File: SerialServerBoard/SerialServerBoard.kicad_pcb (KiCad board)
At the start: 2 copper layers, 60 parts, among them J1 3v3, J2 3v3_SW, J3 1v8, J4 1v35, J5 VCORE, J6 ASSMANN A-DF 09 A/KG-T2S, U1 SG2002, U2 MAX3237EIPWR

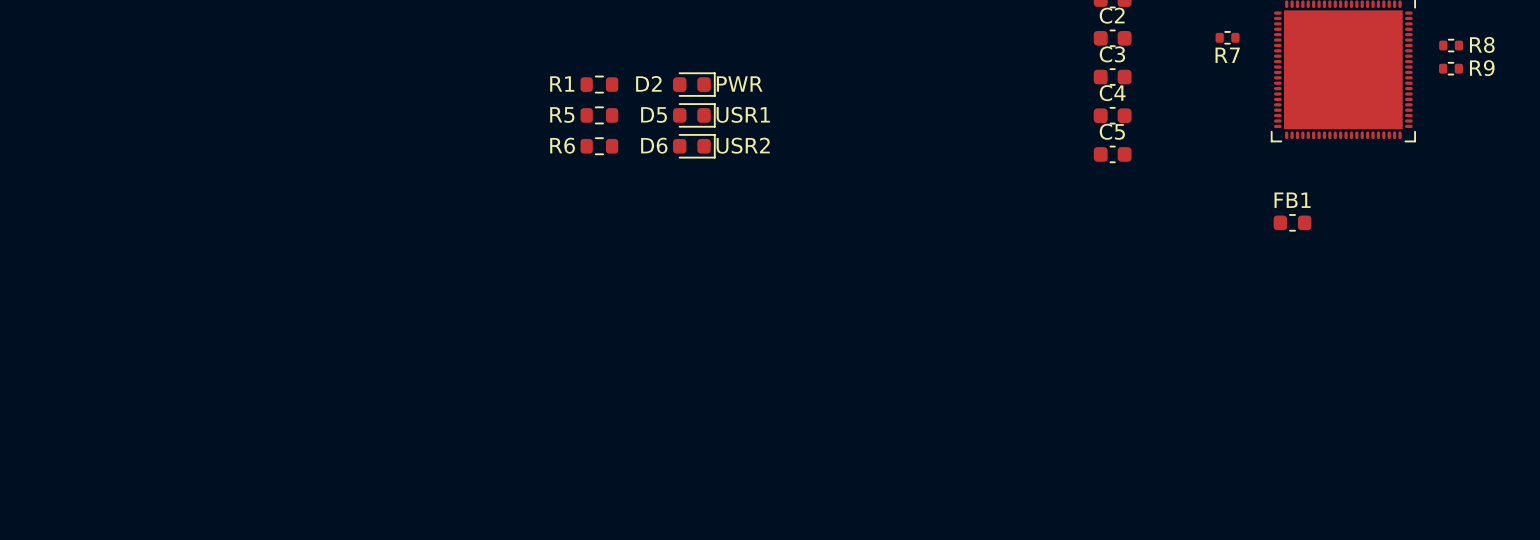
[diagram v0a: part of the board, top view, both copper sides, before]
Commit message: Add ATECC
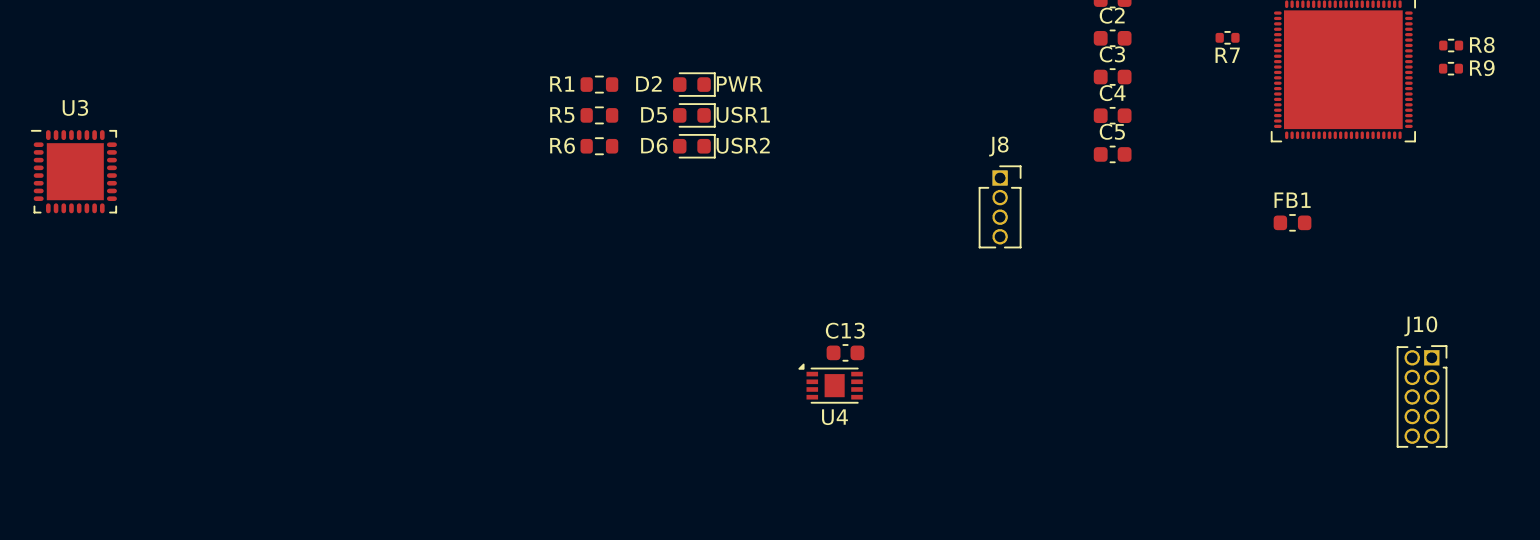
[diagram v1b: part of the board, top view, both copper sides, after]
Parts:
- added C13: TBD, Capacitor_SMD:C_0603_1608Metric, F.Cu at (101.2, 105.4)
- added J10: Conn_ARM_JTAG_SWD_10, Connector_PinSocket_1.27mm:PinSocket_2x05_P1.27mm_Vertical, F.Cu at (139.2, 105.7)
- added J8: ESP UART, Connector_PinSocket_1.27mm:PinSocket_1x04_P1.27mm_Vertical, F.Cu at (111.2, 94.1)
- added U3: ESP32-C3, Footprints:ESP32-C3, F.Cu at (51.2, 93.7)
- added U4: ATECC608B-MAHDA, Package_DFN_QFN:DFN-8-1EP_3x2mm_P0.5mm_EP1.3x1.5mm, F.Cu at (100.5, 107.5)

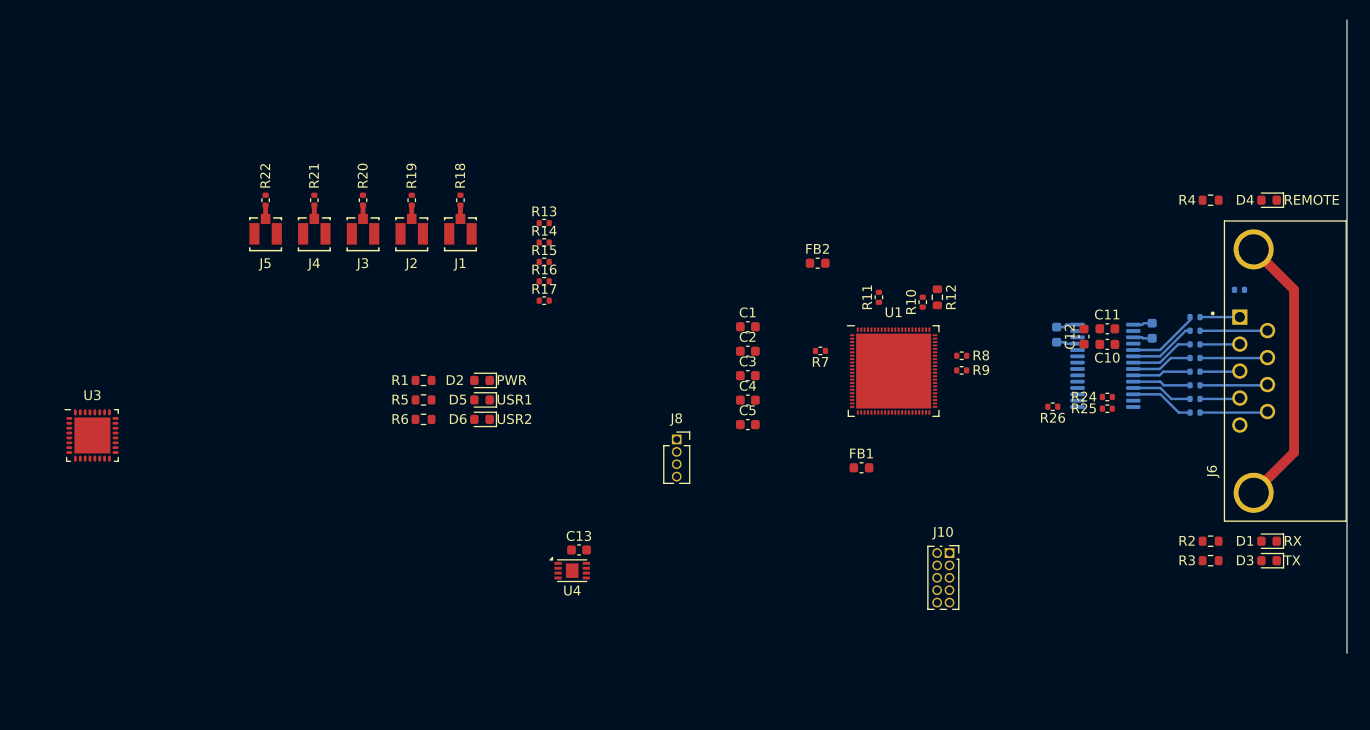
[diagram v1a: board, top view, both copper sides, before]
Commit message: Add micro-SD card slot
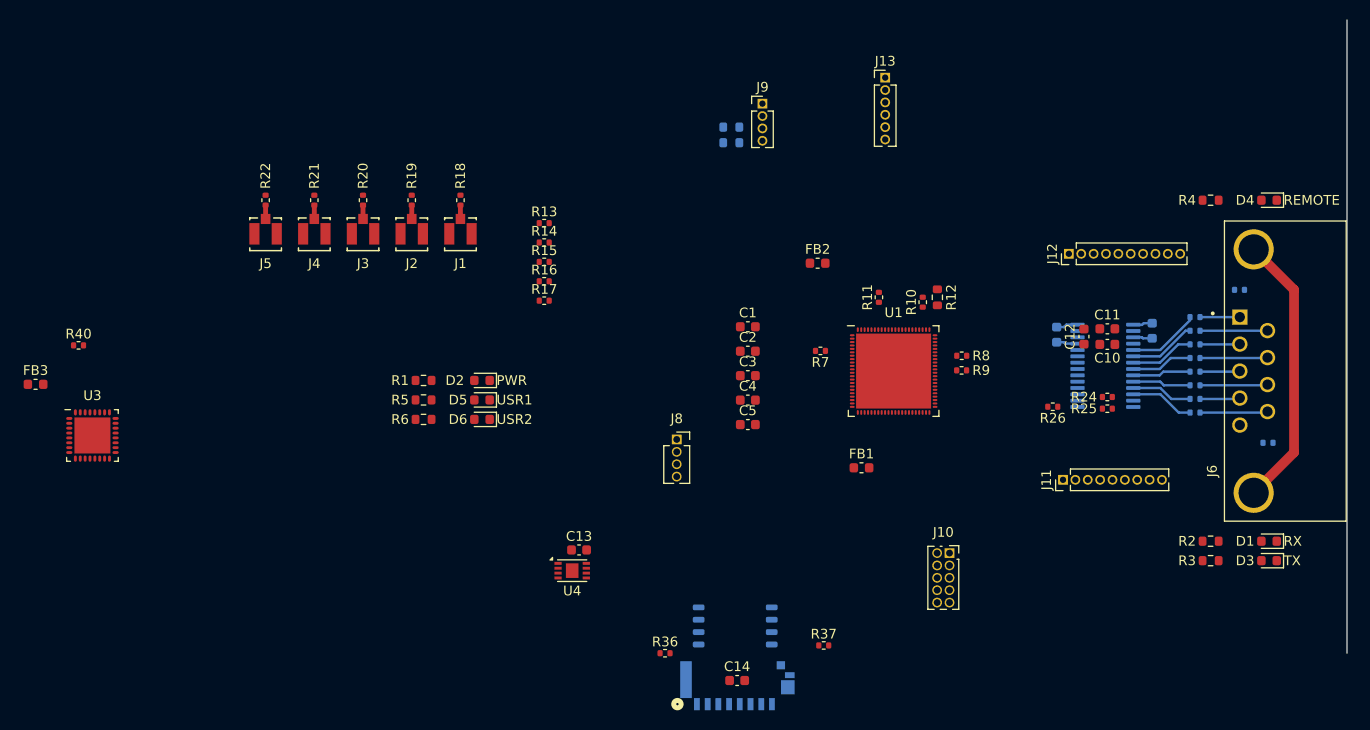
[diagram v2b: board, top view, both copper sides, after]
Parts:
- added C14: TBD, Capacitor_SMD:C_0603_1608Metric, F.Cu at (117.4, 118.8)
- added FB3: FerriteBead_Small, Inductor_SMD:L_0603_1608Metric, F.Cu at (45.4, 88.4)
- added J11: DE9, Connector_PinHeader_1.27mm:PinHeader_1x09_P1.27mm_Vertical, F.Cu at (150.8, 98.2)
- added J12: Control, Connector_PinHeader_1.27mm:PinHeader_1x10_P1.27mm_Vertical, F.Cu at (151.4, 75.0)
- added J13: Comms, Connector_PinHeader_1.27mm:PinHeader_1x06_P1.27mm_Vertical, F.Cu at (132.6, 56.9)
- added J7: Amphenol 10067099-400LF, Footprints:CONN8_10067099-400LF_FCI, B.Cu at (121.9, 121.2)
- added J9: I2C, Connector_PinHeader_1.27mm:PinHeader_1x04_P1.27mm_Vertical, F.Cu at (120.0, 59.6)
- added R35: 0, Resistor_SMD:R_0402_1005Metric, B.Cu at (171.9, 94.4)
- added R36: 0, Resistor_SMD:R_0402_1005Metric, F.Cu at (110.0, 116.0)
- added R37: 0, Resistor_SMD:R_0402_1005Metric, F.Cu at (126.3, 115.2)
- added R38: 4k7, Resistor_SMD:R_0603_1608Metric, B.Cu at (116.8, 63.6)
- added R39: 4k7, Resistor_SMD:R_0603_1608Metric, B.Cu at (116.8, 62.0)
- added R40: 4k7, Resistor_SMD:R_0402_1005Metric, F.Cu at (49.8, 84.4)
- added U5: XTSD01G, Package_LGA:LGA-8_8x6mm_P1.27mm, B.Cu at (117.2, 113.2)
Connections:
- J6 pad 5: GND -> Net-(J6-Pad5)
- U1 pad 10: unconnected-(U1-SD0_D1-Pad10) -> /SoC/SD_D1
- U1 pad 11: unconnected-(U1-SD0_D2-Pad11) -> /SoC/SD_D2
- U1 pad 12: unconnected-(U1-SD0_D3-Pad12) -> /SoC/SD_D3
- U1 pad 14: unconnected-(U1-SD0_CD-Pad14) -> /SoC/SD_CD
- U1 pad 28: unconnected-(U1-IIC0_SCL-Pad28) -> /SoC/I2C_SCL
- U1 pad 29: unconnected-(U1-IIC0_SDA-Pad29) -> /SoC/I2C_SDA
- U1 pad 46: unconnected-(U1-XTAL_OUT-Pad46) -> Net-(U1-XTAL_OUT)
- U1 pad 6: unconnected-(U1-SD0_CLK-Pad6) -> /SoC/SD_CLK
- U1 pad 60: unconnected-(U1-USB_VBUS_DET-Pad60) -> /SoC/USB_DET
- U1 pad 62: unconnected-(U1-PAD_ETH_TXP__EPHY_RXN-Pad62) -> /SoC/ETH_RXN
- U1 pad 63: unconnected-(U1-PAD_ETH_TXM__EPHY_RXP-Pad63) -> /SoC/ETH_RXP
- U1 pad 64: unconnected-(U1-PAD_ETH_RXP__EPHY_TXN-Pad64) -> /SoC/ETH_TXN
- U1 pad 65: unconnected-(U1-PAD_ETH_RXM__EPHY_TXP-Pad65) -> /SoC/ETH_TXP
- U1 pad 69: unconnected-(U1-USB_DP-Pad69) -> /SoC/USB_DP
- U1 pad 7: unconnected-(U1-SD0_CMD-Pad7) -> /SoC/SD_CMD
- U1 pad 70: unconnected-(U1-USB_DM-Pad70) -> /SoC/USB_DM
- U1 pad 8: unconnected-(U1-SD0_D0-Pad8) -> /SoC/SD_D0
- U2 pad 17: unconnected-(U2-DIN5-Pad17) -> /Serial/RS232_RI
- U2 pad 18: unconnected-(U2-ROUT3-Pad18) -> /Serial/RS232_DTR
- U2 pad 19: unconnected-(U2-DIN4-Pad19) -> /Serial/RS232_CTS
- U2 pad 20: unconnected-(U2-ROUT2-Pad20) -> /Serial/RS232_RXD
- U2 pad 21: unconnected-(U2-ROUT1-Pad21) -> /Serial/RS232_RTS
- U2 pad 22: unconnected-(U2-DIN3-Pad22) -> /Serial/RS232_TXD
- U2 pad 23: unconnected-(U2-DIN2-Pad23) -> /Serial/RS232_DSR
- U2 pad 24: unconnected-(U2-DIN1-Pad24) -> /Serial/RS232_DCD
- U3 pad 6: unconnected-(U3-GPIO2-Pad6) -> Net-(U3-GPIO2)
